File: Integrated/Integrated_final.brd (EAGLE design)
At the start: 279.4 x 75.9 mm, 70 parts, among them IC1 74AHC1G32DBV, IC2 74AHC1G08DBV, IC3 74AHC1G08DBV, IC7 74AHC1G32DBV, Q1 PSMN013-30MLC, Q2 PSMN013-30MLC, Q3 PSMN013-30MLC, Q4 PSMN013-30MLC, Q5 PSMN013-30MLC, Q6 PSMN013-30MLC

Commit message: NO DRC ERROR!
YAY
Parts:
- removed R1: 10K, BeagleBone_Black_Wireless:M0805
- moved C10 109.5 mm to (-1.27, 71.1)
- moved JP2 101.7 mm to (-6.35, 55.9), turned to 270 degrees
- moved C1 97.7 mm to (50.8, 76.2)
- moved C3 96.9 mm to (97.8, 31.8), turned to 180 degrees
- moved C11 94.9 mm to (94.0, 33.0), turned to 270 degrees
- moved JP1 94.7 mm to (101.6, 48.3)
- moved JP3 94.7 mm to (106.7, 68.6)
- moved C2 94.1 mm to (45.7, 76.2)
- moved F2 93.3 mm to (2.54, 76.2)
- moved Y2 91.7 mm to (48.3, 71.1)
- moved EXP_TRANS 90.9 mm to (77.5, 59.7)
- moved C7 89.4 mm to (133.3, 33.0), turned to 90 degrees
- moved BREAK/THROTTLE_CONN 86.7 mm to (128.3, 20.3), turned to 0 degrees
- moved U$1 83.8 mm to (66.0, 48.3)
- moved R2 81.9 mm to (-17.8, 29.2)
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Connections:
- net CSC renamed CSC_LOG
- removed net +3V3: JP1.15, JP5.15
- removed net D11(LOG): BRK_CONN.1, JP4.6, Q5.4, R9.2
- removed net N$26: Q3.4, R4.2
- removed net VCC: IC1.5, IC2.5, IC3.5, IC7.5
- new net !RESET_LOG: JP5.16
- new net AREF_LOG: JP5.14
- new net CAN_CS_LOG: JP4.9, LOGG_TRANS.16
- new net CAN_INT_LOG: JP4.10, LOGG_TRANS.12
- new net MISO_LOG: LOGG_TRANS.15, SPI_LCD_CONN.6
- new net MOSI_LOG: LOGG_TRANS.14, SPI_LCD_CONN.8
- new net SCK_LOG: LOGG_TRANS.13, SPI_LCD_CONN.7
- new net SCL_LOG: DASH_IN.4, IC7.1, JP4.11, R12.2
- new net SDA_LOG: DASH_IN.3, JP4.12, Q6.4, R6.2
- new net VBAT_LOG: JP4.1
- new net VBUS_LOG: JP4.3
- net !RESET: no longer JP5.16
- net 3.3V: now also IC1.5, IC2.5, IC3.5, IC7.5, JP5.15; no longer R1.1
- net AREF: no longer JP5.14
- net BRK: now also BRK_CONN.1, JP4.6, Q5.4, R9.2; no longer R1.2
- net CAN_CS: no longer JP4.9, LOGG_TRANS.16
- net CAN_INT: no longer JP4.10, LOGG_TRANS.12
- net D12(LOG): now also Q3.4, R4.2
- net MISO: no longer LOGG_TRANS.15, SPI_LCD_CONN.6
- net MOSI: no longer LOGG_TRANS.14, SPI_LCD_CONN.8
- net SCK: no longer LOGG_TRANS.13, SPI_LCD_CONN.7
- net SCL: no longer DASH_IN.4, IC7.1, JP4.11, R12.2
- net SDA: no longer DASH_IN.3, JP4.12, Q6.4, R6.2
- net VBAT: no longer JP4.1
- net VBUS: no longer JP4.3
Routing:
- net 3.3V: track 31.3 -> 399.8 mm, vias 2 -> 23
- net 12V: track 63.8 -> 280.6 mm, vias 0 -> 3
- net BRK: track 0.00 -> 208.0 mm, vias 0 -> 8
- net D9(LOG): track 0.00 -> 127.1 mm, vias 0 -> 6
- net D10(LOG): track 0.00 -> 125.4 mm, vias 0 -> 7
- net D13(LOG): track 0.00 -> 122.1 mm, vias 0 -> 5
- net SCL_LOG: track 0.00 -> 109.5 mm, vias 0 -> 4
- net CAN+: track 63.0 -> 164.8 mm, vias 0 -> 5
- net SDA_LOG: track 0.00 -> 95.2 mm, vias 0 -> 5
- net EN: track 0.00 -> 76.1 mm, vias 0 -> 1
- net D12(LOG): track 0.00 -> 73.8 mm, vias 0 -> 3
- net RGN_BRK: track 0.00 -> 56.1 mm, vias 0 -> 2
- net N$3: track 0.00 -> 48.0 mm, vias 0 -> 2
- net CAN_INT: track 0.00 -> 46.5 mm, vias 0 -> 4
- net CAN_TX: track 0.00 -> 46.1 mm, vias 0 -> 6
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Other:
- board size 279.4 x 75.9 mm -> 191.8 x 75.9 mm

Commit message: very minor tweak
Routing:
- net CAN_RX: track 42.4 -> 39.3 mm
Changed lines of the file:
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@@
 <contactref element="U$1" pad="4"/>
 <contactref element="LOGG_TRANS" pad="2"/>
-<wire x1="64.135" y1="50.86" x2="64.075" y2="50.8" width="0.4064" layer="1"/>
 <via x="49.53" y="50.8" extent="1-16" drill="0.35"/>
 <wire x1="49.53" y1="50.8" x2="48.26" y2="52.07" width="0.4064" layer="1"/>
 <wire x1="48.26" y1="52.07" x2="48.26" y2="53.6321" width="0.4064" layer="1"/>
-<wire x1="64.135" y1="50.86" x2="64.135" y2="62.865" width="0.4064" layer="1"/>
+<wire x1="64.135" y1="50.86" x2="64.135" y2="52.07" width="0.4064" layer="1"/>
+<wire x1="64.135" y1="52.07" x2="64.135" y2="62.865" width="0.4064" layer="1"/>
 <wire x1="64.135" y1="62.865" x2="64.77" y2="63.5" width="0.4064" layer="1"/>
 <via x="64.77" y="63.5" extent="1-16" drill="0.35"/>
@@
 <via x="71.12" y="63.5" extent="1-16" drill="0.35"/>
 <wire x1="71.12" y1="63.5" x2="72.6821" y2="63.5" width="0.4064" layer="1"/>
-<wire x1="64.135" y1="50.86" x2="63.56" y2="50.86" width="0.4064" layer="1"/>
-<wire x1="63.56" y1="50.86" x2="63.5" y2="50.92" width="0.4064" layer="1"/>
-<wire x1="63.5" y1="50.92" x2="63.5" y2="53.34" width="0.4064" layer="1"/>
-<via x="63.5" y="53.34" extent="1-16" drill="0.35"/>
-<wire x1="63.5" y1="53.34" x2="60.96" y2="50.8" width="0.4064" layer="16"/>
-<wire x1="60.96" y1="50.8" x2="49.53" y2="50.8" width="0.4064" layer="16"/>
+<wire x1="61.6938" y1="50.8" x2="62.9638" y2="52.07" width="0.4064" layer="16"/>
+<via x="62.9638" y="52.07" extent="1-16" drill="0.35"/>
+<wire x1="62.9638" y1="52.07" x2="64.135" y2="52.07" width="0.4064" layer="1"/>
+<wire x1="49.53" y1="50.8" x2="61.6938" y2="50.8" width="0.4064" layer="16"/>
 </signal>
 <signal name="CAN+">

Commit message: A few more minor (but very important) tweaks
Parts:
- moved JP1 15.2 mm to (116.8, 48.3)
- moved JP3 15.2 mm to (121.9, 68.6)
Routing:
- net SCK: track 21.7 -> 37.6 mm
- net EN: track 76.1 -> 92.0 mm
- net MOSI: track 20.4 -> 35.6 mm
- net CAN_INT: track 46.5 -> 61.0 mm, vias 4 -> 3
- net RGN_BRK: track 56.1 -> 41.6 mm
- net THROTTLE: track 39.9 -> 26.1 mm, vias 2 -> 0
- net CAN_CS: track 33.1 -> 46.1 mm, vias 2 -> 1
- net MISO: track 19.9 -> 32.9 mm
- net 3.3V: track 399.8 -> 391.6 mm, vias 23 -> 21
- net BRK: track 208.0 -> 202.9 mm, vias 8 -> 7
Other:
- board text added: "ADALOGGER"
- board text added: "DRIVER CONTROLS"
- board text added: "EXPRESS"
- board text added: "GPS"
- board text added: "LCD"

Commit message: Handing off for charlie's review
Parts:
- added X1, X2: 5566-4, con-molex:5566-4
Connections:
- net A0: now also X2.1
- net A3: now also X2.2
- net A4: now also X2.3
- net D0: now also X2.4
- net D10: now also X1.4
- net D11: now also X1.3
- net D12: now also X1.2
- net D13: now also X1.1
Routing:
- net D0: track 0.00 -> 60.0 mm, vias 0 -> 3
- net D12: track 0.00 -> 55.9 mm, vias 0 -> 1
- net A4: track 0.00 -> 48.3 mm, vias 0 -> 3
- net A3: track 0.00 -> 45.5 mm, vias 0 -> 1
- net D13: track 0.00 -> 45.1 mm, vias 0 -> 3
- net A0: track 0.00 -> 38.0 mm, vias 0 -> 2
- net D10: track 0.00 -> 34.2 mm, vias 0 -> 1
- net D11: track 0.00 -> 33.8 mm, vias 0 -> 1
- net CAN_CS: track 46.1 -> 49.1 mm, vias 1 -> 2
- net RGN_BRK: track 41.6 -> 40.1 mm
- net CAN_INT: vias 3 -> 4
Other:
- board size 191.8 x 75.9 mm -> 201.9 x 77.1 mm
- board text added: "M0_EXPRESS"
- board text added: "SPARE ANALOG"
- board text added: "SPARE DIGITAL"
- board text removed: "DRIVER CONTROLS"
- board text removed: "EXPRESS"
- board text removed: "LCD"

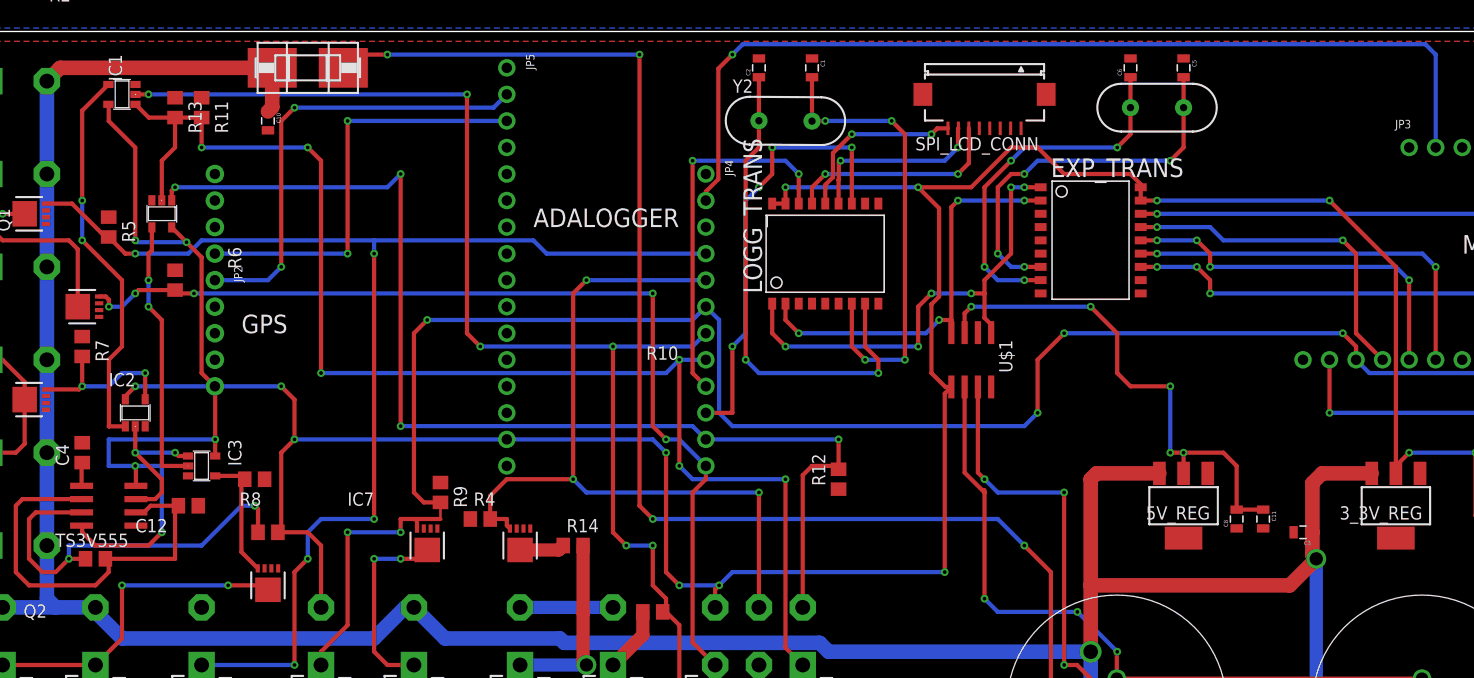
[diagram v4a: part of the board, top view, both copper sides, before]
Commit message: removed some dimensions that were on the copper layer, checked pinning. TODO: fix CAN pinout on the CAN interface connectors, follow linus' BMS issues
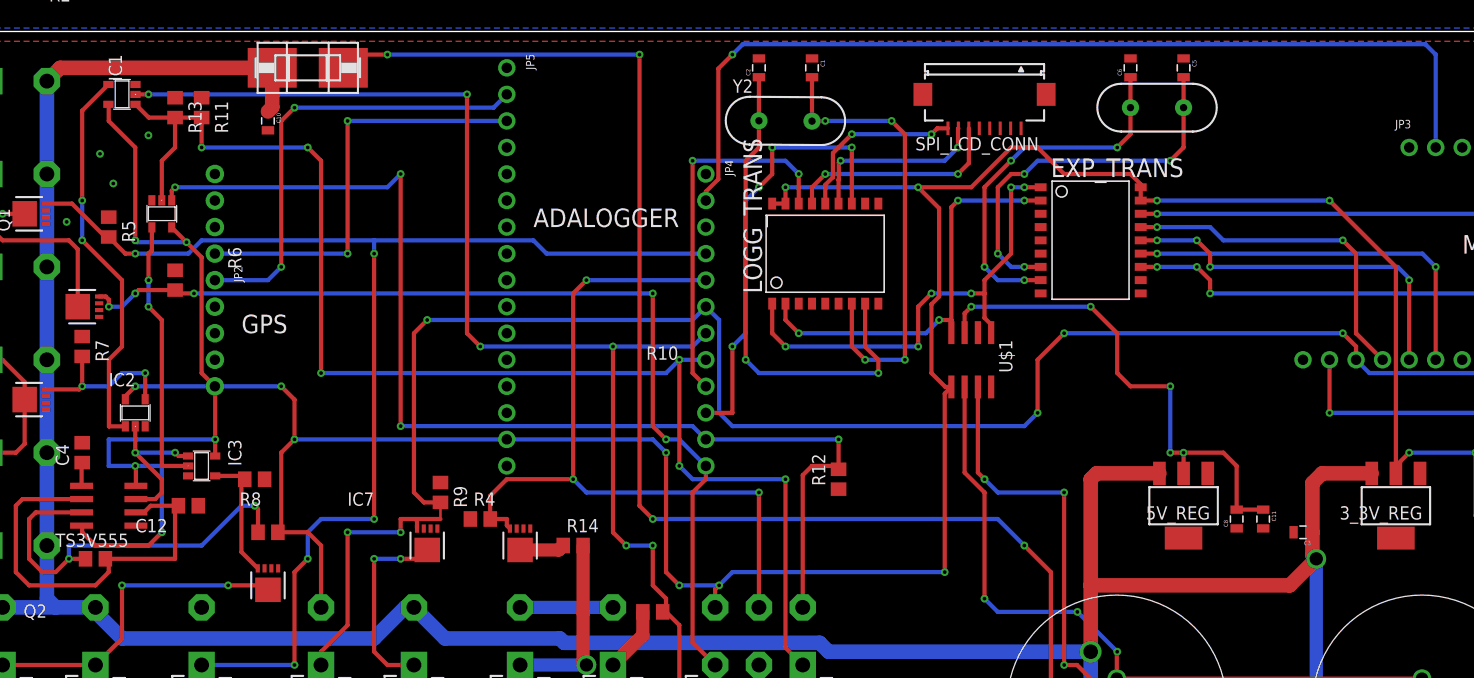
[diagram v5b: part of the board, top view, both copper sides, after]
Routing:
- net SDA_LOG: track 95.2 -> 94.4 mm
- net 12V: track 280.6 -> 280.0 mm
- net GND: vias 0 -> 4
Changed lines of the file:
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@@
 <?xml version="1.0" encoding="utf-8"?>
 <!DOCTYPE eagle SYSTEM "eagle.dtd">
-<eagle version="9.5.2">
+<eagle version="9.1.3">
 <drawing>
 <settings>
@@
 <setting verticaltext="up"/>
 </settings>
-<grid distance="50" unitdist="mil" unit="mil" style="lines" multiple="1" display="no" altdistance="5" altunitdist="mil" altunit="mil"/>
+<grid distance="0.000123031496" unitdist="mil" unit="mil" style="lines" multiple="1" display="no" altdistance="5" altunitdist="mil" altunit="mil"/>
 <layers>
 <layer number="1" name="Top" color="4" fill="1" visible="yes" active="yes"/>
@@
 <dimension x1="78.105" y1="86.36" x2="73.025" y2="66.04" x3="107.95" y3="76.2" textsize="1.778" layer="47" dtype="vertical" unit="inch"/>
 <dimension x1="78.105" y1="63.5" x2="73.025" y2="43.18" x3="107.95" y3="53.34" textsize="1.778" layer="47" dtype="vertical" unit="inch"/>
-<dimension x1="107.95" y1="68.58" x2="107.95" y2="48.26" x3="138.43" y3="58.42" textsize="1.778" layer="21" dtype="vertical" unit="inch"/>
-<dimension x1="40.64" y1="66.04" x2="40.64" y2="76.2" x3="22.86" y3="71.12" textsize="1.778" layer="20"/>
 <dimension x1="241.3" y1="3.81" x2="241.3" y2="80.01" x3="241.3" y3="41.91" textsize="1.778" layer="20" unit="inch"/>
-<dimension x1="-6.35" y1="43.18" x2="19.05" y2="43.18" x3="6.35" y3="66.04" textsize="1.778" layer="21" unit="inch"/>
-<dimension x1="97.79" y1="48.26" x2="107.95" y2="48.26" x3="102.87" y3="68.58" textsize="1.778" layer="1"/>
 <text x="-3.81" y="50.8" size="1.778" layer="21">GPS</text>
 <text x="24.13" y="60.96" size="1.778" layer="21">ADALOGGER</text>
@@
 <wire x1="107.95" y1="48.26" x2="107.95" y2="55.88" width="0.4064" layer="1"/>
 <via x="107.95" y="55.88" extent="1-16" drill="0.35"/>
-<wire x1="106.68" y1="57.15" x2="107.95" y2="55.88" width="0.4064" layer="16"/>
-<wire x1="88.9" y1="57.15" x2="106.68" y2="57.15" width="0.4064" layer="16"/>
+<wire x1="106.855084375" y1="57.15" x2="107.95" y2="56.055084375" width="0.4064" layer="16"/>
+<wire x1="88.9" y1="57.15" x2="106.855084375" y2="57.15" width="0.4064" layer="16"/>
+<wire x1="107.95" y1="56.055084375" x2="107.95" y2="55.88" width="0.4064" layer="16"/>
 </signal>
 <signal name="MISO">
@@
 <wire x1="74.93" y1="50.8" x2="72.39" y2="48.26" width="0.4064" layer="1"/>
 <wire x1="15.24" y1="34.61" x2="15.08" y2="34.45" width="0.4064" layer="1"/>
-<wire x1="15.08" y1="34.45" x2="14.92" y2="34.29" width="0.4064" layer="1"/>
 <wire x1="11.43" y1="31.75" x2="11.43" y2="33.02" width="0.4064" layer="1"/>
 <wire x1="11.43" y1="33.02" x2="12.7" y2="33.02" width="0.4064" layer="1"/>
@@
 <wire x1="31.75" y1="19.05" x2="34.61" y2="21.91" width="1.27" layer="1"/>
 <wire x1="34.61" y1="21.91" x2="34.61" y2="24.13" width="1.27" layer="1"/>
-<wire x1="-1.27" y1="70.22" x2="21.59" y2="76.2" width="0" layer="19" extent="1-1"/>
+<via x="-17.3452" y="67.971034375" extent="1-16" drill="0.35"/>
+<via x="-16.071096875" y="65.132871875" extent="1-16" drill="0.35"/>
+<via x="-12.71209375" y="69.73764375" extent="1-16" drill="0.35"/>
+<via x="-20.53784375" y="61.4551125" extent="1-16" drill="0.35"/>
 </signal>
 <signal name="CAN_L">
@@
 <via x="76.2" y="24.13" extent="1-16" drill="0.35"/>
 <via x="67.31" y="25.4" extent="1-16" drill="0.35"/>
-<wire x1="67.31" y1="35.79225" x2="67.31" y2="35.56" width="0.4064" layer="1"/>
 <wire x1="67.31" y1="35.56" x2="67.31" y2="25.4" width="0.4064" layer="1"/>
 <wire x1="67.31" y1="25.4" x2="68.58" y2="24.13" width="0.4064" layer="16"/>
@@
 <via x="-11.43" y="31.75" extent="1-16" drill="0.35"/>
 <wire x1="-11.43" y1="31.75" x2="-11.43" y2="38.1" width="0.4064" layer="16"/>
-<wire x1="-13.97" y1="36.255" x2="-13.91" y2="36.195" width="0.4064" layer="1"/>
 <via x="-6.32" y="40.64" extent="1-16" drill="0.35"/>
 <wire x1="-6.32" y1="40.64" x2="-16.51" y2="40.64" width="0.4064" layer="16"/>
@@
 <wire x1="100.33" y1="15.24" x2="99.06" y2="16.51" width="1.27" layer="16"/>
 <wire x1="99.06" y1="16.51" x2="99.06" y2="29.21" width="1.27" layer="16"/>
-<wire x1="-0.86" y1="76.2" x2="-1.065" y2="75.995" width="0.4064" layer="1"/>
 <wire x1="77.47" y1="15.24" x2="77.47" y2="20.32" width="1.397" layer="16"/>
 <wire x1="77.47" y1="20.32" x2="52.38435625" y2="20.32" width="1.397" layer="16"/>
@@
 <wire x1="-21.1582" y1="76.2" x2="-0.86" y2="76.2" width="1.397" layer="1"/>
 <wire x1="-26.67" y1="24.5618" x2="-35.56" y2="24.5618" width="1.397" layer="16"/>
-<wire x1="-1.27" y1="75.79" x2="-1.065" y2="75.995" width="1.397" layer="1"/>
 <wire x1="77.47" y1="36.83" x2="78.029" y2="37.389" width="1.397" layer="1"/>
 <wire x1="77.47" y1="20.32" x2="77.47" y2="26.67" width="1.397" layer="1"/>
@@
 <wire x1="-14.92" y1="58.42" x2="-16.35" y2="59.85" width="0.4064" layer="1"/>
 <wire x1="-16.35" y1="59.85" x2="-16.51" y2="60.01" width="0.4064" layer="1"/>
-<wire x1="-16.51" y1="59.69" x2="-16.35" y2="59.85" width="0.4064" layer="1"/>
 <wire x1="-7.62" y1="19.05" x2="1.27" y2="19.05" width="0.4064" layer="16"/>
 <via x="1.27" y="19.05" extent="1-16" drill="0.35"/>
@@
 <contactref element="IC1" pad="4"/>
 <contactref element="IC2" pad="1"/>
-<wire x1="-14.92" y1="41.89" x2="-16.49" y2="41.89" width="0.4064" layer="1"/>
-<wire x1="-16.49" y1="41.89" x2="-16.51" y2="41.91" width="0.4064" layer="1"/>
+<wire x1="-14.92" y1="41.89" x2="-16.45428125" y2="41.89" width="0.4064" layer="1"/>
 <wire x1="-16.49" y1="41.89" x2="-16.49" y2="48.28" width="0.4064" layer="1"/>
 <wire x1="-16.49" y1="48.28" x2="-15.24" y2="49.53" width="0.4064" layer="1"/>
@@
 <wire x1="-15.24" y1="49.53" x2="-15.24" y2="55.88" width="0.4064" layer="1"/>
 <wire x1="-15.24" y1="55.88" x2="-19.05" y2="59.69" width="0.4064" layer="1"/>
+<wire x1="-16.45428125" y1="41.89" x2="-16.49" y2="41.89" width="0.4064" layer="1"/>
 </signal>
 <signal name="N$29">
@@
 <via x="29.21" y="19.05" extent="1-16" drill="1.27" diameter="1.397"/>
 <wire x1="28.89" y1="30.48" x2="28.89" y2="24.00075" width="1.27" layer="1"/>
-<wire x1="28.89" y1="24.00075" x2="28.8544" y2="23.96515" width="0.4064" layer="1"/>
 <wire x1="29.21" y1="19.05" x2="22.86" y2="19.05" width="1.27" layer="16"/>
 <wire x1="29.21" y1="19.05" x2="28.89" y2="19.37" width="1.27" layer="1"/>
@@
 <contactref element="R14" pad="1"/>
 <contactref element="Q3" pad="MB"/>
-<wire x1="26.67" y1="30.48" x2="26.99" y2="30.48" width="0.4064" layer="1"/>
 <wire x1="26.99" y1="30.48" x2="26.565" y2="30.055" width="1.27" layer="1"/>
 <wire x1="26.565" y1="30.055" x2="22.86" y2="30.055" width="1.27" layer="1"/>
@@
 <wire x1="39.37" y1="35.56" x2="40.64" y2="36.83" width="0.4064" layer="1"/>
 <wire x1="40.64" y1="36.83" x2="40.64" y2="38.1" width="0.4064" layer="1"/>
-<wire x1="-10.16" y1="54.61" x2="-10.16" y2="54.93" width="0.4064" layer="1"/>
 <wire x1="40.64" y1="38.1" x2="38.1" y2="40.64" width="0.4064" layer="16"/>
 <wire x1="38.1" y1="40.64" x2="36.83" y2="40.64" width="0.4064" layer="16"/>
@@
 <wire x1="35.56" y1="41.91" x2="35.56" y2="54.61" width="0.4064" layer="1"/>
 <via x="35.56" y="54.61" extent="1-16" drill="0.35"/>
-<wire x1="-10.16" y1="54.93" x2="-10.48" y2="54.61" width="0.4064" layer="1"/>
 <wire x1="-17.425" y1="54.315" x2="-16.805" y2="54.315" width="0.4064" layer="1"/>
 <via x="-13.97" y="54.61" extent="1-16" drill="0.35"/>
@@
 <mfgpreviewcolor name="substratecolor" color="0xFF786E46"/>
 </mfgpreviewcolors>
-<errors>
-</errors>
 </board>
 </drawing>

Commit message: ok i think its finally done
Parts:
- removed F2: SMD-MICRO-FUSE-BLOCK, f-lf-omniblok-s:OMNIBLOK
- added F1: SMD-MICRO-FUSE-BLOCK, f-lf-omniblok-s:OMNIBLOK
- added R1, R15: 0, rcl:R0805
- moved C10 86.2 mm to (79.7, 41.5), turned to 90 degrees
- moved CAN_CONN_OUT 3.97 mm to (73.5, 14.7)
- moved JP5 1.50 mm to (20.1, 57.2)
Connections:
- removed net CAN+: CAN_CONN_IN.4, CAN_CONN_OUT.4, F2.P$1
- new net CAN_SHIELD: CAN_CONN_OUT.1, R15.2
- new net CAN_SHIELD_2: CAN_CONN_IN.1, R1.2
- net 12V: now also CAN_CONN_IN.2, CAN_CONN_OUT.2, F1.P$1, F1.P$2; no longer CAN_CONN_IN.1, CAN_CONN_OUT.1, F2.P$2
- net CAN_H: now also CAN_CONN_IN.4, CAN_CONN_OUT.4; no longer CAN_CONN_IN.5, CAN_CONN_OUT.5
- net CAN_L: now also CAN_CONN_IN.5, CAN_CONN_OUT.5; no longer CAN_CONN_IN.2, CAN_CONN_OUT.2
- net GND: now also R1.1, R15.1
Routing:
- net CAN+: track 164.8 -> 0.00 mm, vias 5 -> 0
- net CAN_L: track 67.7 -> 86.3 mm, vias 3 -> 4
- net CAN_SHIELD_2: track 0.00 -> 16.1 mm, vias 0 -> 2
- net 12V: track 280.0 -> 265.6 mm
- net CAN_H: track 82.2 -> 96.2 mm, vias 5 -> 7
- net CAN_SHIELD: track 0.00 -> 13.0 mm, vias 0 -> 1
- net RX: track 40.6 -> 39.2 mm
- net TX: track 43.5 -> 42.0 mm
